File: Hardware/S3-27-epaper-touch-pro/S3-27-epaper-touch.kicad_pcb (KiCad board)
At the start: 4 copper layers, 65.4 x 71 mm, 61 parts, among them J1 AFC24-S24FIC-00, J2 USB_C_Programming, J3 Conn_01x06, J4 Conn_01x06_Female, J5 Groove sensor, J6 Conn_01x06, Q1 Si1308, Q2 BC817, Q3 BC817, U1 ESP32-S3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

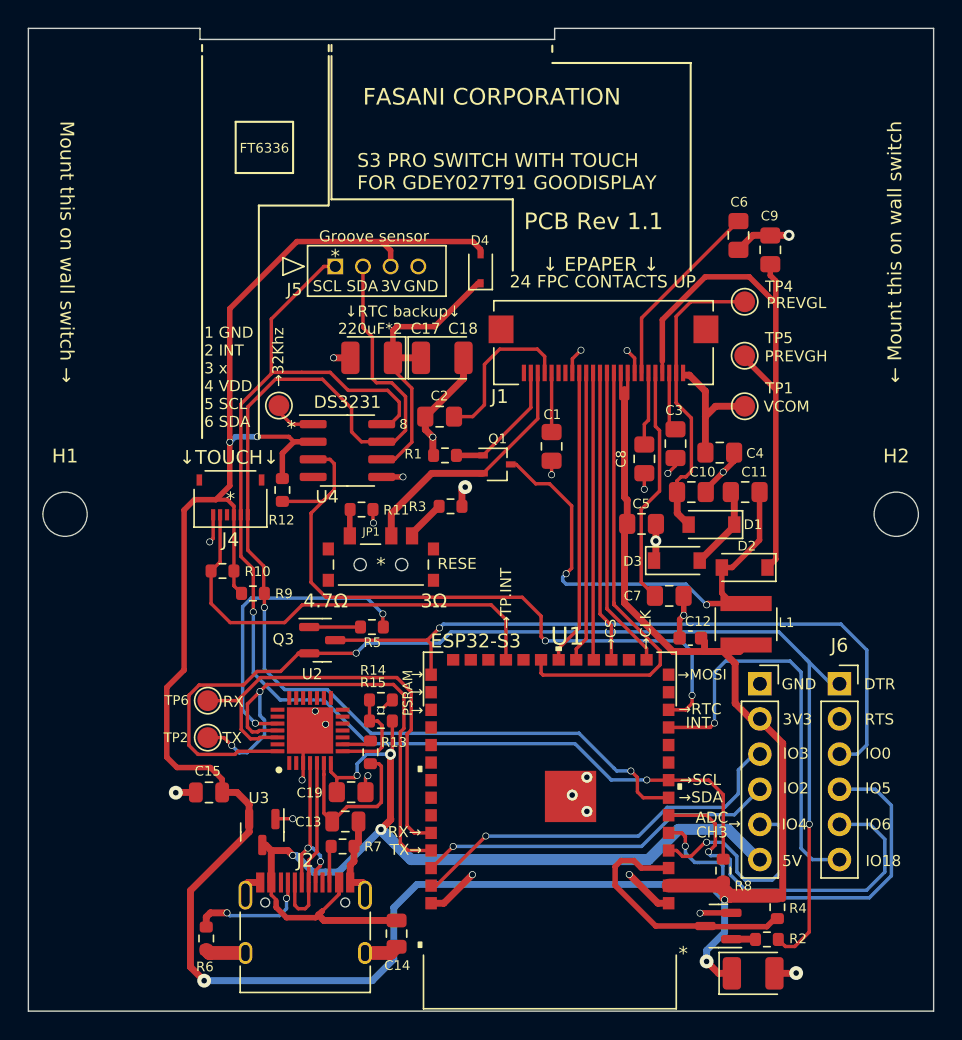
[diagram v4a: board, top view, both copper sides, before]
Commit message: S3 update to review: No more C 220uF RTC backup use CR1220
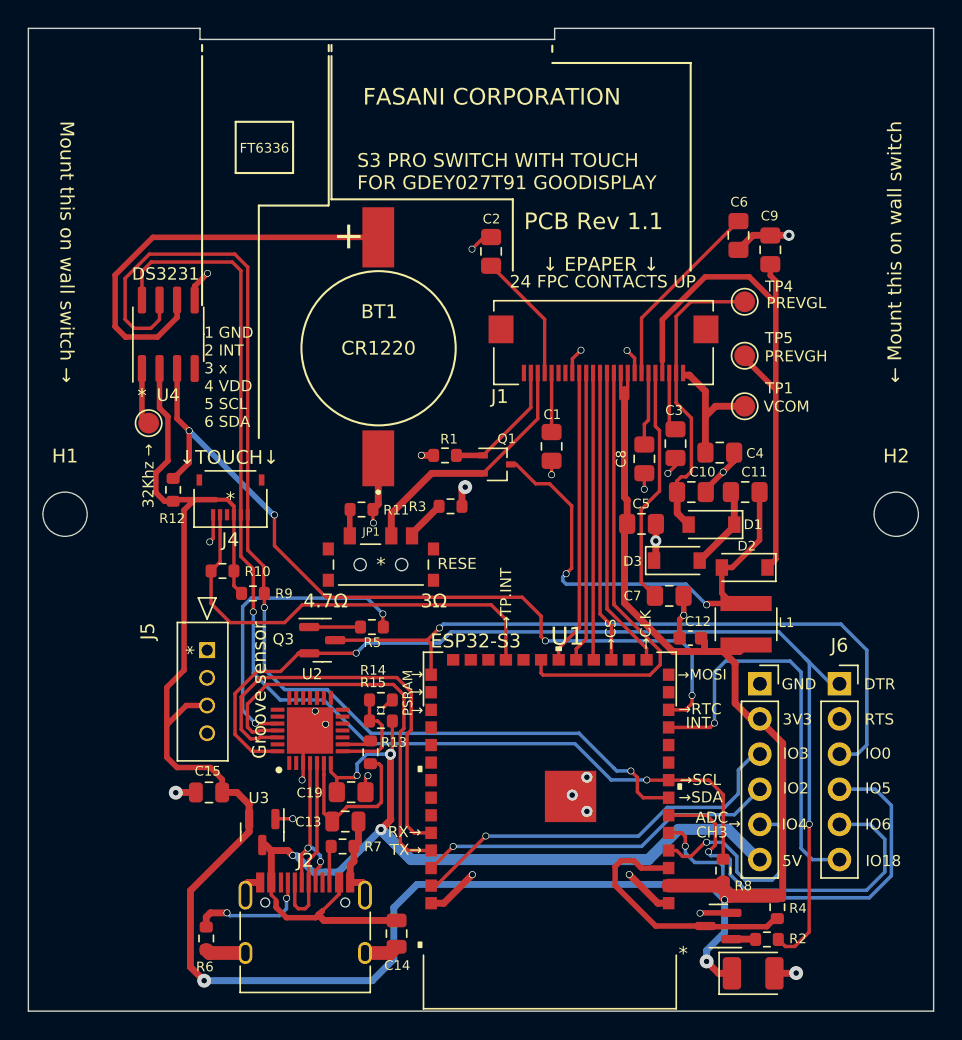
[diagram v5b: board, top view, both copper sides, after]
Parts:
- removed C17, C18: 220uF, Capacitor_Tantalum_SMD:CP_EIA-3528-21_Kemet-B
- removed D4: 1N5819WS, Diode_SMD:D_SOD-323
- removed TP2: TX, TestPoint:TestPoint_Pad_D1.5mm
- removed TP6: RX, TestPoint:TestPoint_Pad_D1.5mm
- added BT1: CR1220, footprint:CR12202ZX, F.Cu at (130.1, 77.9)
- J5: footprint footprint:MOLEX-I2C-532530470 -> footprint:MOLEX-I2C-Groove
- moved J5 29.2 mm to (117.7, 99.9), turned to -90 degrees
- moved U4 15.4 mm to (114.9, 77.1), turned to 90 degrees
- moved C2 12.5 mm to (138.2, 71.1), turned to -90 degrees
- moved TP3 9.50 mm to (113.5, 83.5)
- moved R12 7.89 mm to (115.3, 88.3), turned to 90 degrees
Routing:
- net +3V3: track 209.9 -> 179.7 mm, vias 5 -> 3
- net Net-(BT1-Pad1): track 21.1 -> 30.5 mm
- net /3231_INT: track 51.1 -> 59.5 mm, vias 2 -> 4
- net RX: track 37.8 -> 29.5 mm, vias 2 -> 0
- net /DTR: track 84.2 -> 77.0 mm
- net /TOUCH_SDA: track 82.0 -> 87.9 mm
- net TX: track 32.9 -> 30.3 mm
- net GND: track 67.6 -> 65.2 mm
- net Net-(C2-Pad2): track 11.7 -> 9.35 mm
- net /TOUCH_SCL: track 87.7 -> 86.3 mm
- net Net-(TP3-Pad1): track 3.30 -> 4.15 mm
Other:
- board text added: "+"
- board text added: "32Khz →"
- board text added: "CR1220"
- board text removed: "220uF*2"
- board text removed: "3V"
- board text removed: "8"
- board text removed: "RX"
- board text removed: "SCL"
- board text removed: "SDA"
- board text removed: "TX"
- board text removed: "→32Khz"
- board text removed: "↓RTC backup↓"

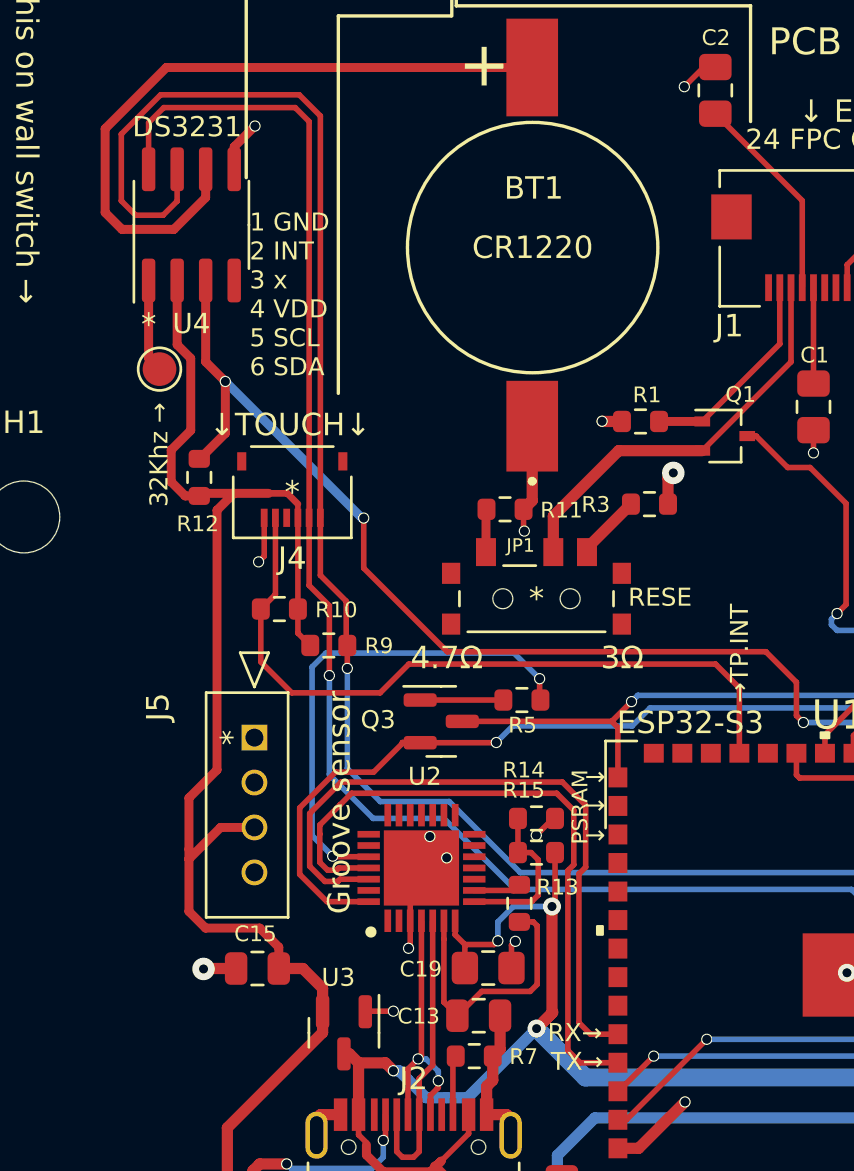
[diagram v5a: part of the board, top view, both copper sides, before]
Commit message: Update S3 heading to 1.1 release
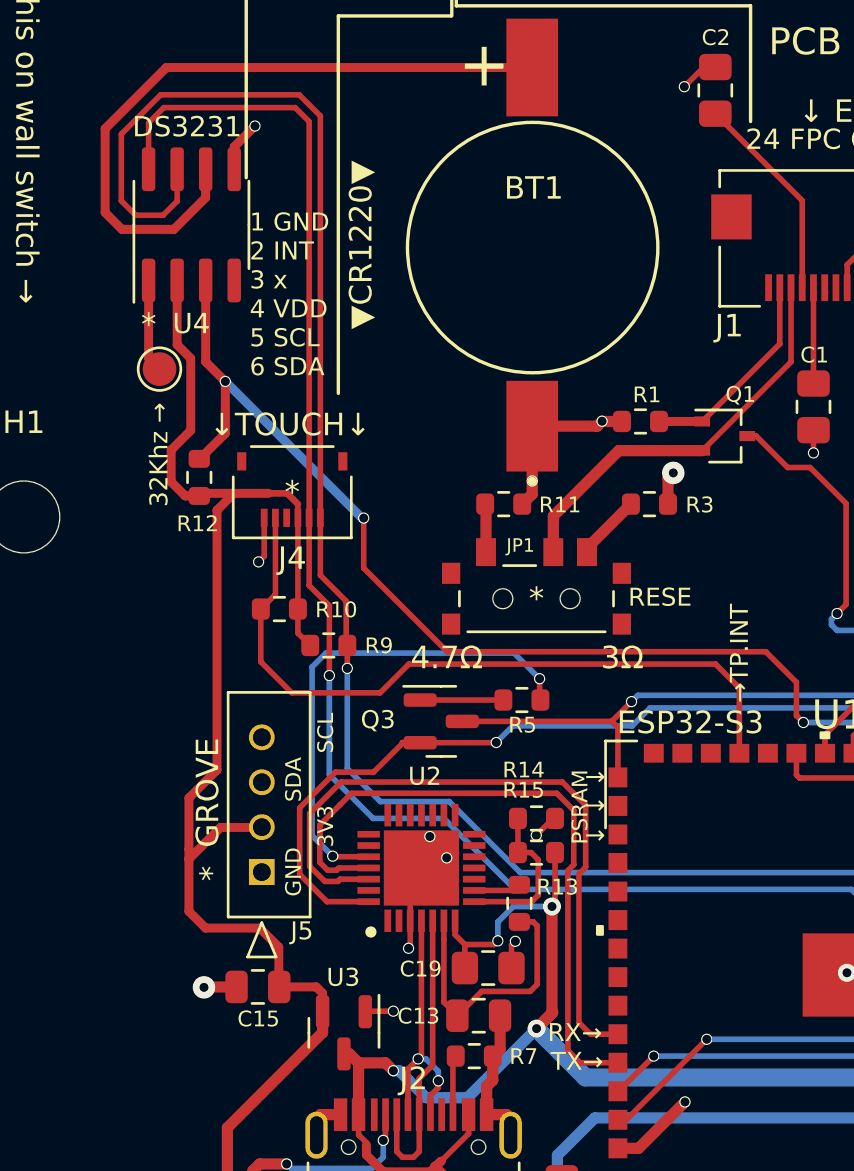
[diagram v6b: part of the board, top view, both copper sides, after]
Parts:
- J5: value Groove sensor -> GROVE
- moved J5 6.00 mm to (118.0, 105.9), turned to 90 degrees
- moved C15 0.82 mm to (117.9, 111.0)
- moved R11 0.24 mm to (128.8, 89.5)
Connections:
- J5 pad 1: /TOUCH_SCL -> GND
- J5 pad 2: /TOUCH_SDA -> +3V3
- J5 pad 3: +3V3 -> /TOUCH_SDA
- J5 pad 4: GND -> /TOUCH_SCL
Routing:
- net GND: track 65.2 -> 67.2 mm
- net +3V3: track 179.7 -> 180.4 mm
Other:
- board text added: "GROVE"
- board text added: "SCL"
- board text added: "SDA"
- board text added: "github.com/martinberlin/bistable-smart-switch"
- board text added: "■ DS3231 INT→IO8 (Pulled-up w/R12) ■ I2C: SDA→IO7 SCL→IO15 ■"
- board text added: "▼CR1220▼"
- board text removed: "CR1220"
- board text removed: "■ DS3231 INT → IO8 (Pulled-up w/R12) ■ I2C → SDA IO7 → SCL IO15 ■ 5V / 3V3 are power in pins. 5V input is VBUS ► U3 LDO ► 3.3V"
